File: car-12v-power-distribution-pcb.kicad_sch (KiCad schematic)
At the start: 7 parts, among them J1 IN_BATT, J2 IN_ACC, J3 OUT_DASHCAM, J4 OUT_PHONE, J5 OUT_BOOST, J6 OUT_SPARE1, J7 OUT_SPARE2

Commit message: Reset to blank KiCad 6 schematic and PCB
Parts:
- removed J1: IN_BATT, PicoSpoX:PicoSpoX_1x02_P3.00mm_SMD, symbol Connector_Generic:Conn_01x02
- removed J2: IN_ACC, PicoSpoX:PicoSpoX_1x02_P3.00mm_SMD, symbol Connector_Generic:Conn_01x02
- removed J3: OUT_DASHCAM, PicoSpoX:PicoSpoX_1x03_P3.00mm_SMD, symbol Connector_Generic:Conn_01x03
- removed J4: OUT_PHONE, PicoSpoX:PicoSpoX_1x03_P3.00mm_SMD, symbol Connector_Generic:Conn_01x03
- removed J5: OUT_BOOST, PicoSpoX:PicoSpoX_1x03_P3.00mm_SMD, symbol Connector_Generic:Conn_01x03
- removed J6: OUT_SPARE1, PicoSpoX:PicoSpoX_1x03_P3.00mm_SMD, symbol Connector_Generic:Conn_01x03
- removed J7: OUT_SPARE2, PicoSpoX:PicoSpoX_1x03_P3.00mm_SMD, symbol Connector_Generic:Conn_01x03
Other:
- note removed: "+12V_ACC"
- note removed: "+12V_BATT"
- note removed: "GND"
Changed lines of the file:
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@@
     (title "Car 12V Power Distribution")
     (date "2026-02-28")
-    (rev "B")
+    (rev "C")
   )
-  (symbol (lib_id "Connector_Generic:Conn_01x02") (at 40 40 0) (unit 1)
-    (in_bom yes) (on_board yes)
-    (property "Reference" "J1" (at 40 35 0) (effects (font (size 1 1))))
-    (property "Value" "IN_BATT" (at 40 45 0) (effects (font (size 1 1))))
-    (property "Footprint" "PicoSpoX:PicoSpoX_1x02_P3.00mm_SMD" (at 0 0 0) (effects (font (size 1 1))))
-    (property "Datasheet" "" (at 0 0 0) (effects (font (size 1 1))))
-    (property "Description" "2-pin 12V battery input" (at 0 0 0) (effects (font (size 1 1))))
-    (pin "1")
-    (pin "2")
-  )
-  (symbol (lib_id "Connector_Generic:Conn_01x02") (at 40 80 0) (unit 1)
-    (in_bom yes) (on_board yes)
-    (property "Reference" "J2" (at 40 75 0) (effects (font (size 1 1))))
-    (property "Value" "IN_ACC" (at 40 85 0) (effects (font (size 1 1))))
-    (property "Footprint" "PicoSpoX:PicoSpoX_1x02_P3.00mm_SMD" (at 0 0 0) (effects (font (size 1 1))))
-    (property "Datasheet" "" (at 0 0 0) (effects (font (size 1 1))))
-    (property "Description" "2-pin accessory 12V input" (at 0 0 0) (effects (font (size 1 1))))
-    (pin "1")
-    (pin "2")
-  )
-  (symbol (lib_id "Connector_Generic:Conn_01x03") (at 120 30 0) (unit 1)
-    (in_bom yes) (on_board yes)
-    (property "Reference" "J3" (at 120 25 0) (effects (font (size 1 1))))
-    (property "Value" "OUT_DASHCAM" (at 120 35 0) (effects (font (size 1 1))))
-    (property "Footprint" "PicoSpoX:PicoSpoX_1x03_P3.00mm_SMD" (at 0 0 0) (effects (font (size 1 1))))
-    (property "Datasheet" "" (at 0 0 0) (effects (font (size 1 1))))
-    (property "Description" "3-pin output: BATT/ACC/GND" (at 0 0 0) (effects (font (size 1 1))))
-    (pin "1")
-    (pin "2")
-    (pin "3")
-  )
-  (symbol (lib_id "Connector_Generic:Conn_01x03") (at 120 60 0) (unit 1)
-    (in_bom yes) (on_board yes)
-    (property "Reference" "J4" (at 120 55 0) (effects (font (size 1 1))))
-    (property "Value" "OUT_PHONE" (at 120 65 0) (effects (font (size 1 1))))
-    (property "Footprint" "PicoSpoX:PicoSpoX_1x03_P3.00mm_SMD" (at 0 0 0) (effects (font (size 1 1))))
-    (property "Datasheet" "" (at 0 0 0) (effects (font (size 1 1))))
-    (property "Description" "3-pin output: BATT/ACC/GND" (at 0 0 0) (effects (font (size 1 1))))
-    (pin "1")
-    (pin "2")
-    (pin "3")
-  )
-  (symbol (lib_id "Connector_Generic:Conn_01x03") (at 120 90 0) (unit 1)
-    (in_bom yes) (on_board yes)
-    (property "Reference" "J5" (at 120 85 0) (effects (font (size 1 1))))
-    (property "Value" "OUT_BOOST" (at 120 95 0) (effects (font (size 1 1))))
-    (property "Footprint" "PicoSpoX:PicoSpoX_1x03_P3.00mm_SMD" (at 0 0 0) (effects (font (size 1 1))))
-    (property "Datasheet" "" (at 0 0 0) (effects (font (size 1 1))))
-    (property "Description" "3-pin output: BATT/ACC/GND" (at 0 0 0) (effects (font (size 1 1))))
-    (pin "1")
-    (pin "2")
-    (pin "3")
-  )
-  (symbol (lib_id "Connector_Generic:Conn_01x03") (at 120 120 0) (unit 1)
-    (in_bom yes) (on_board yes)
-    (property "Reference" "J6" (at 120 115 0) (effects (font (size 1 1))))
-    (property "Value" "OUT_SPARE1" (at 120 125 0) (effects (font (size 1 1))))
-    (property "Footprint" "PicoSpoX:PicoSpoX_1x03_P3.00mm_SMD" (at 0 0 0) (effects (font (size 1 1))))
-    (property "Datasheet" "" (at 0 0 0) (effects (font (size 1 1))))
-    (property "Description" "3-pin output: BATT/ACC/GND" (at 0 0 0) (effects (font (size 1 1))))
-    (pin "1")
-    (pin "2")
-    (pin "3")
-  )
-  (symbol (lib_id "Connector_Generic:Conn_01x03") (at 120 150 0) (unit 1)
-    (in_bom yes) (on_board yes)
-    (property "Reference" "J7" (at 120 145 0) (effects (font (size 1 1))))
-    (property "Value" "OUT_SPARE2" (at 120 155 0) (effects (font (size 1 1))))
-    (property "Footprint" "PicoSpoX:PicoSpoX_1x03_P3.00mm_SMD" (at 0 0 0) (effects (font (size 1 1))))
-    (property "Datasheet" "" (at 0 0 0) (effects (font (size 1 1))))
-    (property "Description" "3-pin output: BATT/ACC/GND" (at 0 0 0) (effects (font (size 1 1))))
-    (pin "1")
-    (pin "2")
-    (pin "3")
-  )
-  (wire (pts (xy 45 40) (xy 70 40)) (stroke (width 0) (type default)))
-  (wire (pts (xy 70 40) (xy 70 30)) (stroke (width 0) (type default)))
-  (wire (pts (xy 70 30) (xy 115 30)) (stroke (width 0) (type default)))
-  (wire (pts (xy 70 30) (xy 70 60)) (stroke (width 0) (type default)))
-  (wire (pts (xy 70 60) (xy 115 60)) (stroke (width 0) (type default)))
-  (wire (pts (xy 70 60) (xy 70 90)) (stroke (width 0) (type default)))
-  (wire (pts (xy 70 90) (xy 115 90)) (stroke (width 0) (type default)))
-  (wire (pts (xy 70 90) (xy 70 120)) (stroke (width 0) (type default)))
-  (wire (pts (xy 70 120) (xy 115 120)) (stroke (width 0) (type default)))
-  (wire (pts (xy 70 120) (xy 70 150)) (stroke (width 0) (type default)))
-  (wire (pts (xy 70 150) (xy 115 150)) (stroke (width 0) (type default)))
-  (wire (pts (xy 45 80) (xy 75 80)) (stroke (width 0) (type default)))
-  (wire (pts (xy 75 80) (xy 75 32.54)) (stroke (width 0) (type default)))
-  (wire (pts (xy 75 32.54) (xy 115 32.54)) (stroke (width 0) (type default)))
-  (wire (pts (xy 75 32.54) (xy 75 62.54)) (stroke (width 0) (type default)))
-  (wire (pts (xy 75 62.54) (xy 115 62.54)) (stroke (width 0) (type default)))
-  (wire (pts (xy 75 62.54) (xy 75 92.54)) (stroke (width 0) (type default)))
-  (wire (pts (xy 75 92.54) (xy 115 92.54)) (stroke (width 0) (type default)))
-  (wire (pts (xy 75 92.54) (xy 75 122.54)) (stroke (width 0) (type default)))
-  (wire (pts (xy 75 122.54) (xy 115 122.54)) (stroke (width 0) (type default)))
-  (wire (pts (xy 75 122.54) (xy 75 152.54)) (stroke (width 0) (type default)))
-  (wire (pts (xy 75 152.54) (xy 115 152.54)) (stroke (width 0) (type default)))
-  (wire (pts (xy 45 42.54) (xy 80 42.54)) (stroke (width 0) (type default)))
-  (wire (pts (xy 45 82.54) (xy 80 82.54)) (stroke (width 0) (type default)))
-  (wire (pts (xy 80 42.54) (xy 80 34.54)) (stroke (width 0) (type default)))
-  (wire (pts (xy 80 34.54) (xy 115 34.54)) (stroke (width 0) (type default)))
-  (wire (pts (xy 80 34.54) (xy 80 64.54)) (stroke (width 0) (type default)))
-  (wire (pts (xy 80 64.54) (xy 115 64.54)) (stroke (width 0) (type default)))
-  (wire (pts (xy 80 64.54) (xy 80 94.54)) (stroke (width 0) (type default)))
-  (wire (pts (xy 80 94.54) (xy 115 94.54)) (stroke (width 0) (type default)))
-  (wire (pts (xy 80 94.54) (xy 80 124.54)) (stroke (width 0) (type default)))
-  (wire (pts (xy 80 124.54) (xy 115 124.54)) (stroke (width 0) (type default)))
-  (wire (pts (xy 80 124.54) (xy 80 154.54)) (stroke (width 0) (type default)))
-  (wire (pts (xy 80 154.54) (xy 115 154.54)) (stroke (width 0) (type default)))
-  (text "+12V_BATT" (at 72 20 0) (effects (font (size 1 1) (thickness 0.15))))
-  (text "+12V_ACC" (at 78 20 0) (effects (font (size 1 1) (thickness 0.15))))
-  (text "GND" (at 84 20 0) (effects (font (size 1 1) (thickness 0.15))))
 )

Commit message: version 1.0
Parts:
- added D1: LED, symbol Device:LED
- added D2, D3: LED, LED_SMD:LED_0805_2012Metric, symbol Device:LED
- added H1: MountingHole, symbol Mechanical:MountingHole
- added H2, H3, H4: MountingHole, MountingHole:MountingHole_2.7mm_M2.5, symbol Mechanical:MountingHole
- added J1, J3, J4: Conn_01x04, molex-picospox-0874370231_01x04:CONN_874370231-SD_04_MOL, symbol Connector_Generic:Conn_01x04
- added J2, J5, J6, J7: Conn_01x03, molex-picospox-0874370231_01x03:CONN_874370231-SD_03_MOL, symbol Connector_Generic:Conn_01x03
- added R1, R2, R3: 500, Resistor_SMD:R_0603_1608Metric, symbol Device:R
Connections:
- new net: D3.1 (K), R3.1
- new net: D2.1 (K), R2.1
- new net: D1.1 (K), R1.1
- new net +12V: D1.2 (A), J1.1 (Pin_1), J2.1 (Pin_1), J3.1 (Pin_1), J4.1 (Pin_1), J5.1 (Pin_1), J6.1 (Pin_1), J7.1 (Pin_1)
- new net 12V_ACC: D2.2 (A), J1.2 (Pin_2), J2.2 (Pin_2), J3.2 (Pin_2), J4.2 (Pin_2), J5.2 (Pin_2), J6.2 (Pin_2), J7.2 (Pin_2)
- new net 12V_HEADLIGHT: D3.2 (A), J1.3 (Pin_3), J3.3 (Pin_3), J4.3 (Pin_3)
- new net GND: J1.4 (Pin_4), J2.3 (Pin_3), J3.4 (Pin_4), J4.4 (Pin_4), J5.3 (Pin_3), J6.3 (Pin_3), J7.3 (Pin_3), R1.2, R2.2, R3.2
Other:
- note added: "12v -> led has ~ 2.7v drop -> we want 20mA so that's 12-2.7=9.3v -> V = IR; R = V/I = 9.3V/.02 = 465 ~= 500"
- note added: "BOOST-GAUGE"
- note added: "DASHCAM"
- note added: "INPUT"
- note added: "INTAKE-AIR-TEMP"
- note added: "LED MONITOR"
- note added: "PHONE CHARGER"
- note added: "SPARE"

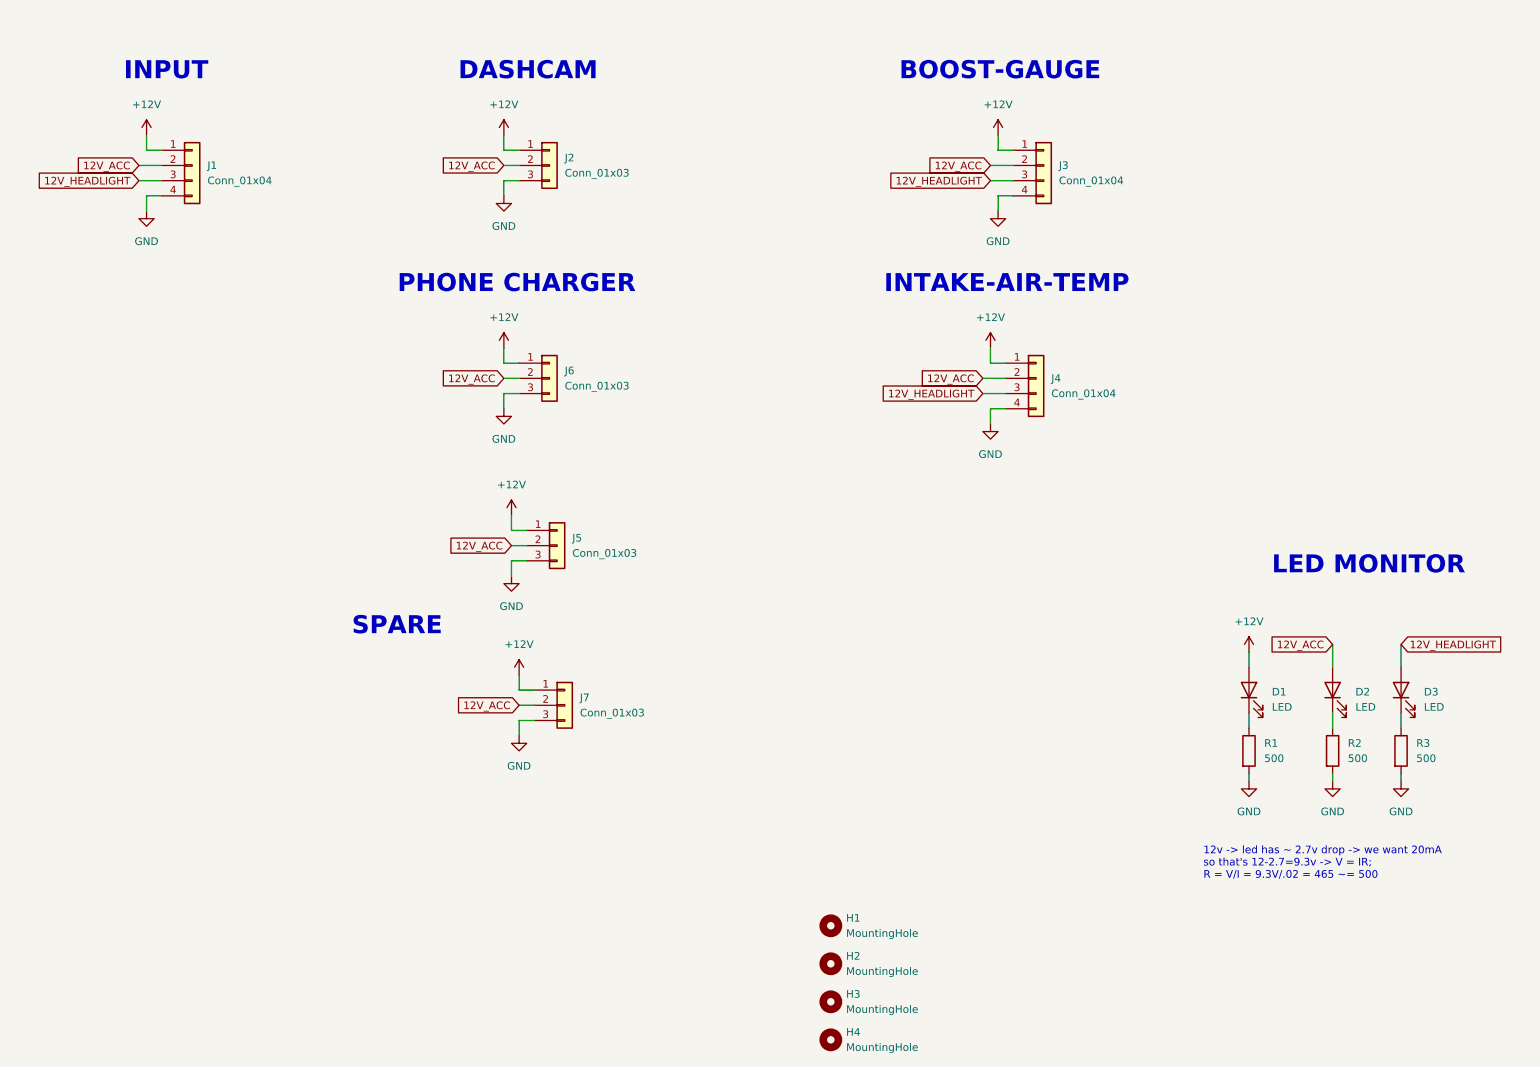
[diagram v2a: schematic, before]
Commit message: updated grounding hole
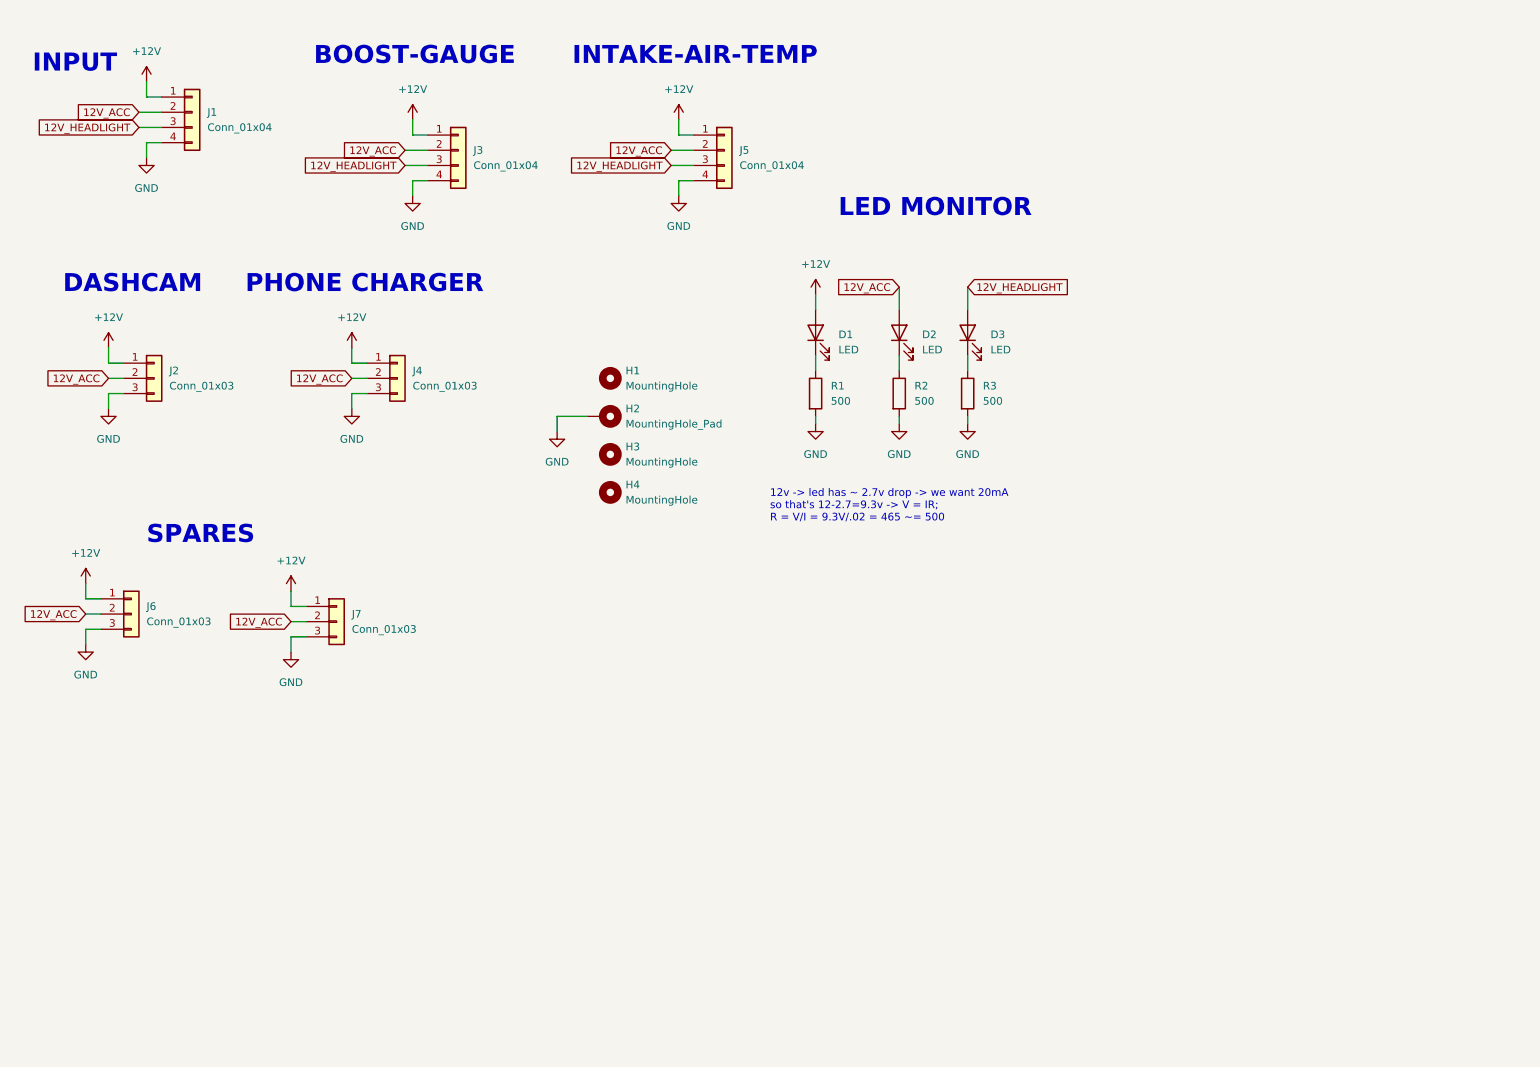
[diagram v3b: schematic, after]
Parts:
- removed H2: MountingHole, MountingHole:MountingHole_2.7mm_M2.5, symbol Mechanical:MountingHole
- added H2: MountingHole_Pad, MountingHole:MountingHole_2.5mm_Pad_TopBottom, symbol Mechanical:MountingHole_Pad
- D1: footprint (none) -> LED_SMD:LED_0603_1608Metric
- D2, D3: footprint LED_SMD:LED_0805_2012Metric -> LED_SMD:LED_0603_1608Metric
- H1: footprint (none) -> MountingHole:MountingHole_2.7mm_M2.5
- renumbered J6 to J4, J4 to J5, J5 to J6
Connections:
- net GND: now also H2.1
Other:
- note added: "SPARES"
- note removed: "SPARE"
- moved on the sheet: D1, D2, D3, H1, H3, H4, J1, J2, J3, J4, J5, J6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
